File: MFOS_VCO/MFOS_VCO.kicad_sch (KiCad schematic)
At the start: 65 parts, among them J1 Conn_02x05_Odd_Even, J10 Jack-DC, J11 Jack-DC, J12 Conn_01x04, J13 Conn_01x02, J14 Conn_01x02, J15 Conn_01x04, J2 Jack-DC, J20 Jack-DC, J24 Conn_01x03, J26 Conn_01x03, J3 Jack-DC, J4 Jack-DC, J5 Jack-DC, J6 Jack-DC, J7 Jack-DC, J8 Jack-DC, J9 Jack-DC, Q1 PN4391, U1 OP275, U2 TL072, U3 SSM2212, U4 TL074, U5 LM13700, U6 TL072

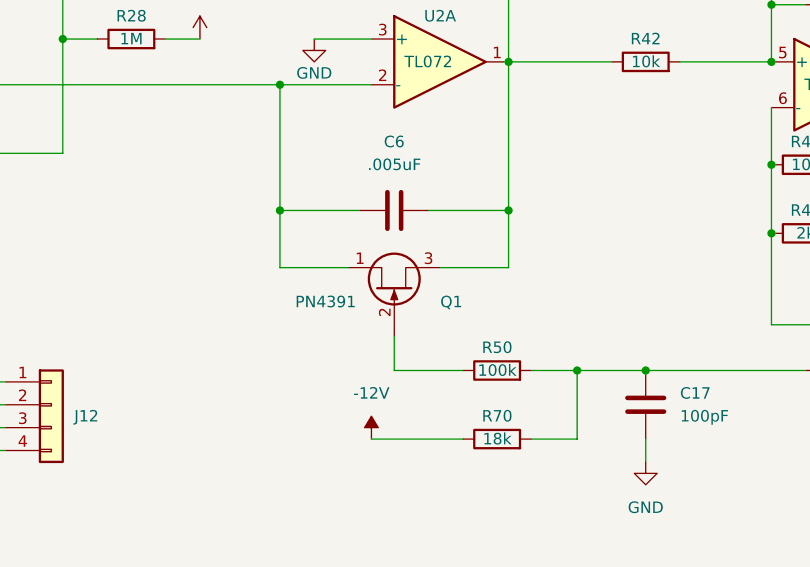
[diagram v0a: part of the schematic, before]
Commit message: Fixed PN4391 bug. Made some layout changes. Fitted molex connectors instead of pin connectors
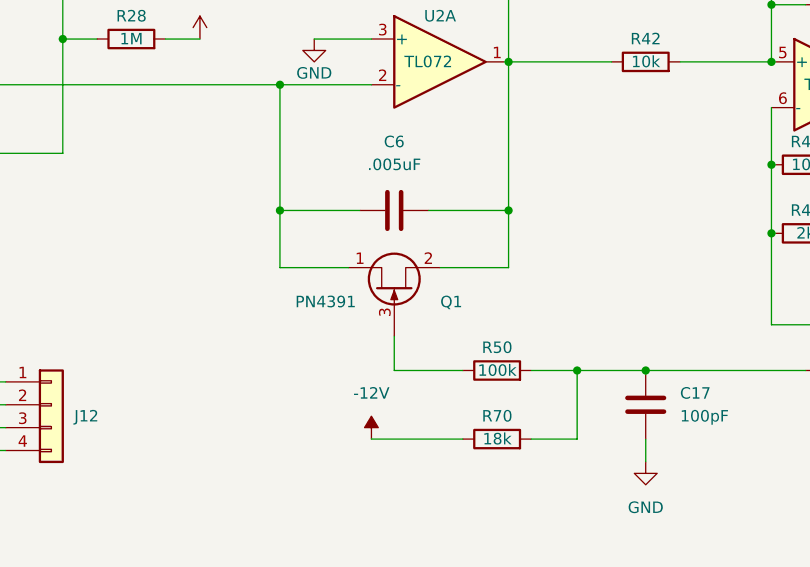
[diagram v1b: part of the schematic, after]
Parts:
- J12, J15: footprint Connector_PinHeader_2.54mm:PinHeader_1x04_P2.54mm_Vertical -> Connector_Molex:Molex_KK-254_AE-6410-04A_1x04_P2.54mm_Vertical
- J13, J14: footprint Connector_PinHeader_2.54mm:PinHeader_1x02_P2.54mm_Vertical -> Connector_Molex:Molex_KK-254_AE-6410-02A_1x02_P2.54mm_Vertical
- J24, J26: footprint Connector_PinHeader_2.54mm:PinHeader_1x03_P2.54mm_Vertical -> Connector_Molex:Molex_KK-254_AE-6410-03A_1x03_P2.54mm_Vertical
- Q1: symbol Device:Q_NJFET_DGS -> dhk:PN4391
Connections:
- net RAW: now also Q1.2 (S); no longer Q1.3 (S)
- net at R50.1: now also Q1.3 (G); no longer Q1.2 (G)
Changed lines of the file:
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@@
       (effects (font (size 1.27 1.27)) (justify left) hide)
     )
-    (property "Footprint" "Connector_PinHeader_2.54mm:PinHeader_1x02_P2.54mm_Vertical" (id 2) (at 63.5 133.35 0)
+    (property "Footprint" "Connector_Molex:Molex_KK-254_AE-6410-02A_1x02_P2.54mm_Vertical" (id 2) (at 63.5 133.35 0)
       (effects (font (size 1.27 1.27)) hide)
     )
@@
       (effects (font (size 1.27 1.27)) (justify left) hide)
     )
-    (property "Footprint" "Connector_PinHeader_2.54mm:PinHeader_1x04_P2.54mm_Vertical" (id 2) (at 107.95 142.24 0)
+    (property "Footprint" "Connector_Molex:Molex_KK-254_AE-6410-04A_1x04_P2.54mm_Vertical" (id 2) (at 107.95 142.24 0)
       (effects (font (size 1.27 1.27)) hide)
     )
@@
     (pin "8")
   )
-  (symbol (lib_id "Device:Q_NJFET_DGS") (at 193.04 129.54 90) (unit 1)
+  (symbol (lib_id "dhk:PN4391") (at 193.04 129.54 90) (unit 1)
     (in_bom yes) (on_board yes)
     (property "Reference" "Q1" (id 0) (at 199.39 130.81 90))
@@
       (effects (font (size 1.27 1.27)) hide)
     )
-    (property "Datasheet" "https://my.centralsemi.com/datasheets/PN4391-4393.PDF" (id 3) (at 193.04 129.54 0)
+    (property "Datasheet" "~" (id 3) (at 193.04 129.54 0)
       (effects (font (size 1.27 1.27)) hide)
     )
@@
       (effects (font (size 1.27 1.27)) (justify left) hide)
     )
-    (property "Footprint" "Connector_PinHeader_2.54mm:PinHeader_1x02_P2.54mm_Vertical" (id 2) (at 57.15 162.56 0)
+    (property "Footprint" "Connector_Molex:Molex_KK-254_AE-6410-02A_1x02_P2.54mm_Vertical" (id 2) (at 57.15 162.56 0)
       (effects (font (size 1.27 1.27)) hide)
     )
@@
       (effects (font (size 1.27 1.27)) (justify left) hide)
     )
-    (property "Footprint" "Connector_PinHeader_2.54mm:PinHeader_1x03_P2.54mm_Vertical" (id 2) (at 105.41 52.07 0)
+    (property "Footprint" "Connector_Molex:Molex_KK-254_AE-6410-03A_1x03_P2.54mm_Vertical" (id 2) (at 105.41 52.07 0)
       (effects (font (size 1.27 1.27)) hide)
     )
@@
       (effects (font (size 1.27 1.27)) (justify left) hide)
     )
-    (property "Footprint" "Connector_PinHeader_2.54mm:PinHeader_1x03_P2.54mm_Vertical" (id 2) (at 105.41 39.37 0)
+    (property "Footprint" "Connector_Molex:Molex_KK-254_AE-6410-03A_1x03_P2.54mm_Vertical" (id 2) (at 105.41 39.37 0)
       (effects (font (size 1.27 1.27)) hide)
     )
@@
       (effects (font (size 1.27 1.27)) (justify left) hide)
     )
-    (property "Footprint" "Connector_PinHeader_2.54mm:PinHeader_1x04_P2.54mm_Vertical" (id 2) (at 154.94 142.24 0)
+    (property "Footprint" "Connector_Molex:Molex_KK-254_AE-6410-04A_1x04_P2.54mm_Vertical" (id 2) (at 154.94 142.24 0)
       (effects (font (size 1.27 1.27)) hide)
     )
@@
     )
     (path "/7acdccd5-5114-469a-a864-4d03b27a06bc/a2ba3d86-b784-41bc-a290-3490c56f0b8d"
-      (reference "C12") (unit 1) (value "1uF") (footprint "Capacitor_THT:CP_Radial_D8.0mm_P3.50mm")
+      (reference "C12") (unit 1) (value "1uF") (footprint "Capacitor_THT:CP_Radial_D5.0mm_P2.00mm")
     )
     (path "/7acdccd5-5114-469a-a864-4d03b27a06bc/5b8f82f7-50ed-489c-a5e8-c0e3253695fd"
-      (reference "C13") (unit 1) (value "1uF") (footprint "Capacitor_THT:CP_Radial_D8.0mm_P3.50mm")
+      (reference "C13") (unit 1) (value "1uF") (footprint "Capacitor_THT:CP_Radial_D5.0mm_P2.50mm")
     )
     (path "/7acdccd5-5114-469a-a864-4d03b27a06bc/f76b011a-7175-4705-974b-7cf75e9e4dac"
@@
     )
     (path "/c87e57f2-b7e1-4d6f-ba2b-cf1b29cbb78a"
-      (reference "J12") (unit 1) (value "Conn_01x04") (footprint "Connector_PinHeader_2.54mm:PinHeader_1x04_P2.54mm_Vertical")
+      (reference "J12") (unit 1) (value "Conn_01x04") (footprint "Connector_Molex:Molex_KK-254_AE-6410-04A_1x04_P2.54mm_Vertical")
     )
     (path "/10837bbd-a474-4d5a-b45d-6d8d91870528"
-      (reference "J13") (unit 1) (value "Conn_01x02") (footprint "Connector_PinHeader_2.54mm:PinHeader_1x02_P2.54mm_Vertical")
+      (reference "J13") (unit 1) (value "Conn_01x02") (footprint "Connector_Molex:Molex_KK-254_AE-6410-02A_1x02_P2.54mm_Vertical")
     )
     (path "/9264d64e-4464-4e65-b3be-3378b389b494"
-      (reference "J14") (unit 1) (value "Conn_01x02") (footprint "Connector_PinHeader_2.54mm:PinHeader_1x02_P2.54mm_Vertical")
+      (reference "J14") (unit 1) (value "Conn_01x02") (footprint "Connector_Molex:Molex_KK-254_AE-6410-02A_1x02_P2.54mm_Vertical")
     )
     (path "/1edc5437-6f24-4db0-b7c3-a15a255b4826"
-      (reference "J15") (unit 1) (value "Conn_01x04") (footprint "Connector_PinHeader_2.54mm:PinHeader_1x04_P2.54mm_Vertical")
+      (reference "J15") (unit 1) (value "Conn_01x04") (footprint "Connector_Molex:Molex_KK-254_AE-6410-04A_1x04_P2.54mm_Vertical")
     )
     (path "/08bde9de-ce04-4a90-b4a1-091de9485729"
@@
     )
     (path "/c26ac3ea-f984-4b04-95ef-660e34a65c0b"
-      (reference "J24") (unit 1) (value "Conn_01x03") (footprint "Connector_PinHeader_2.54mm:PinHeader_1x03_P2.54mm_Vertical")
+      (reference "J24") (unit 1) (value "Conn_01x03") (footprint "Connector_Molex:Molex_KK-254_AE-6410-03A_1x03_P2.54mm_Vertical")
     )
     (path "/b9c577c0-fa11-4c91-afcb-69ccd1d37ee0"
-      (reference "J26") (unit 1) (value "Conn_01x03") (footprint "Connector_PinHeader_2.54mm:PinHeader_1x03_P2.54mm_Vertical")
+      (reference "J26") (unit 1) (value "Conn_01x03") (footprint "Connector_Molex:Molex_KK-254_AE-6410-03A_1x03_P2.54mm_Vertical")
     )
     (path "/7acdccd5-5114-469a-a864-4d03b27a06bc/cf6744c7-c8df-4b13-86b1-1b1d7aa15581"

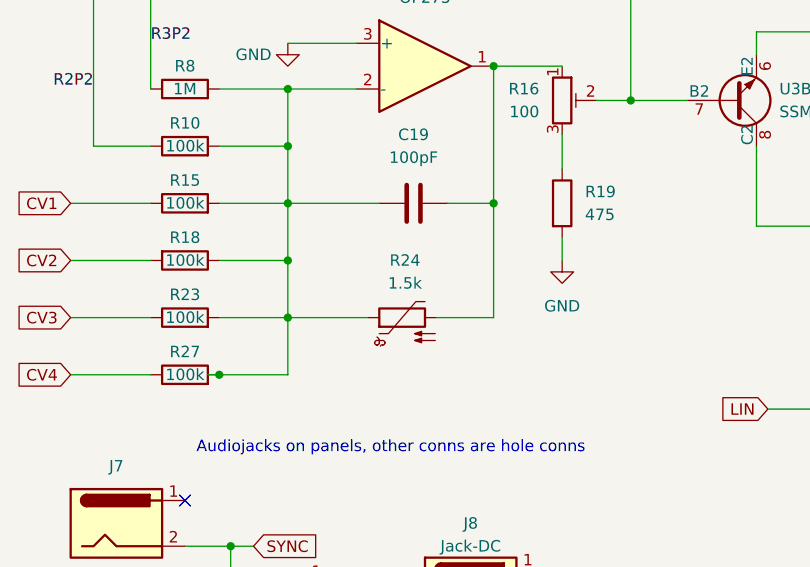
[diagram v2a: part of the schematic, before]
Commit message: Removed R24 from BOM (bought separately) " ;
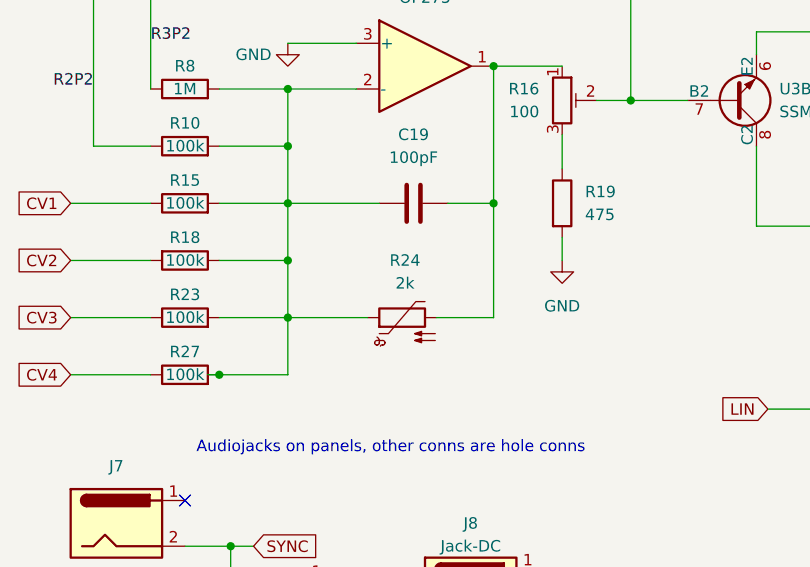
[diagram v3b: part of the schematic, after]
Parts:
- R24: value 1.5k -> 2k; now left out of the parts list
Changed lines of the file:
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@@
   )
   (symbol (lib_id "Device:Thermistor_PTC") (at 69.85 104.14 90) (unit 1)
-    (in_bom yes) (on_board yes) (fields_autoplaced)
+    (in_bom no) (on_board yes) (fields_autoplaced)
     (property "Reference" "R24" (id 0) (at 70.1675 97.79 90))
-    (property "Value" "1.5k" (id 1) (at 70.1675 100.33 90))
+    (property "Value" "2k" (id 1) (at 70.1675 100.33 90))
     (property "Footprint" "Resistor_THT:R_Axial_DIN0207_L6.3mm_D2.5mm_P7.62mm_Horizontal" (id 2) (at 74.93 102.87 0)
       (effects (font (size 1.27 1.27)) (justify left) hide)
@@
     )
     (path "/f1b4db0c-a110-42f6-b38d-9b3a743d2359"
-      (reference "R24") (unit 1) (value "1.5k") (footprint "Resistor_THT:R_Axial_DIN0207_L6.3mm_D2.5mm_P7.62mm_Horizontal")
+      (reference "R24") (unit 1) (value "2k") (footprint "Resistor_THT:R_Axial_DIN0207_L6.3mm_D2.5mm_P7.62mm_Horizontal")
     )
     (path "/7acdccd5-5114-469a-a864-4d03b27a06bc/079cc3b0-ee23-4203-8236-a80325b5e4b0"
